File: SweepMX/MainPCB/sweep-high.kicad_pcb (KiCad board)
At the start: 2 copper layers, 229.5 x 95.2 mm, 61 parts, among them J1 AudioJack4dpb, J2 AudioJack4dpb, SW10 SW_Push, SW10_r1 SW_Push, SW11 SW_Push, SW11_r1 SW_Push, SW12 SW_Push, SW12_r1 SW_Push, SW13_r1 SW_Push, SW14 SW_Push, SW14_r1 SW_Push, SW15 SW_Push, SW15_r1 SW_Push, SW16 SW_Push, SW16_r1 SW_Push, SW17 SW_Push, SW17_r1 SW_Push, SW18 SW_Push, SW18_r1 SW_Push, SW2 SW_Push, SW20 SW_Push, SW21 SW_Push, SW2_r1 SW_Push, SW3 SW_Push, SW3_r1 SW_Push, SW4 SW_Push, SW4_r1 SW_Push, SW5 SW_Push, SW5_r1 SW_Push, SW6 SW_Push, SW6_r1 SW_Push, SW7_r1 SW_Push, SW8 SW_Push, SW8_r1 SW_Push, SW9 SW_Push, SW9_r1 SW_Push, U1 ProMicro-kbd, U2 ProMicro-kbd

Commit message: rename of some bits and a couple missed fixes
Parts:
- moved J1 0.12 mm to (149.6, 121.8)
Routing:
- net Switch15: track 48.6 -> 56.1 mm
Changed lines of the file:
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@@
   )
   (footprint "env_extra:PJ-320A" (layer "F.Cu")
-    (at 149.55 121.925 180)
+    (at 149.55 121.8 180)
     (property "Sheetfile" "sweep-high.kicad_sch")
     (property "Sheetname" "")
@@
   )
   (footprint "env_extra:PJ-320A" (layer "F.Cu")
-    (at 150.975 117.45)
+    (at 150.975 117.4)
     (property "Sheetfile" "sweep-high.kicad_sch")
     (property "Sheetname" "")
@@
   (segment (start 146.160165 83.45) (end 146.160165 89.302765) (width 0.15) (layer "B.Cu") (net 2))
   (segment (start 146.160165 89.302765) (end 147.7054 90.848) (width 0.15) (layer "B.Cu") (net 2))
-  (segment (start 143.08 94.488) (end 143.08 100.76) (width 0.25) (layer "F.Cu") (net 3))
   (segment (start 140.56 103.28) (end 140.56 114.964) (width 0.25) (layer "F.Cu") (net 3))
-  (segment (start 142.064 93.472) (end 143.08 94.488) (width 0.25) (layer "F.Cu") (net 3))
+  (segment (start 143.08 100.76) (end 140.56 103.28) (width 0.25) (layer "F.Cu") (net 3))
   (segment (start 138.938 93.472) (end 142.064 93.472) (width 0.25) (layer "F.Cu") (net 3))
-  (segment (start 152.90924 93.388) (end 159.275 99.75376) (width 0.25) (layer "F.Cu") (net 3))
-  (segment (start 159.275 117.3) (end 159.125 117.45) (width 0.25) (layer "F.Cu") (net 3))
-  (segment (start 159.275 99.75376) (end 159.275 117.3) (width 0.25) (layer "F.Cu") (net 3))
+  (segment (start 142.064 93.472) (end 143.08 94.488) (width 0.25) (layer "F.Cu") (net 3))
   (segment (start 140.56 114.964) (end 141.225 115.629) (width 0.25) (layer "F.Cu") (net 3))
-  (segment (start 141.225 115.629) (end 141.225 121.75) (width 0.25) (layer "F.Cu") (net 3))
-  (segment (start 141.225 121.75) (end 141.4 121.925) (width 0.25) (layer "F.Cu") (net 3))
-  (segment (start 143.08 100.76) (end 140.56 103.28) (width 0.25) (layer "F.Cu") (net 3))
+  (segment (start 152.90924 93.388) (end 159.275 99.75376) (width 0.25) (layer "F.Cu") (net 3))
+  (segment (start 141.225 115.629) (end 141.225 121.625) (width 0.25) (layer "F.Cu") (net 3))
+  (segment (start 159.275 99.75376) (end 159.275 117.25) (width 0.25) (layer "F.Cu") (net 3))
+  (segment (start 141.225 121.625) (end 141.4 121.8) (width 0.25) (layer "F.Cu") (net 3))
+  (segment (start 159.275 117.25) (end 159.125 117.4) (width 0.25) (layer "F.Cu") (net 3))
+  (segment (start 143.08 94.488) (end 143.08 100.76) (width 0.25) (layer "F.Cu") (net 3))
   (via (at 138.938 93.472) (size 0.6) (drill 0.35) (layers "F.Cu" "B.Cu") (net 3))
   (segment (start 138.938 93.472) (end 138.854 93.388) (width 0.25) (layer "B.Cu") (net 3))
   (segment (start 138.854 93.388) (end 132.4854 93.388) (width 0.25) (layer "B.Cu") (net 3))
   (segment (start 140.038 88.308) (end 147.7054 88.308) (width 0.25) (layer "F.Cu") (net 4))
-  (segment (start 136.4 117.525) (end 137.3 116.625) (width 0.25) (layer "F.Cu") (net 4))
+  (segment (start 136.4 117.4) (end 137.3 116.5) (width 0.25) (layer "F.Cu") (net 4))
   (segment (start 137.3 91.046) (end 140.038 88.308) (width 0.25) (layer "F.Cu") (net 4))
-  (segment (start 137.3 116.625) (end 137.3 91.046) (width 0.25) (layer "F.Cu") (net 4))
+  (segment (start 137.3 116.5) (end 137.3 91.046) (width 0.25) (layer "F.Cu") (net 4))
   (segment (start 127.45 116.5) (end 129.092 116.5) (width 0.25) (layer "F.Cu") (net 5))
   (segment (start 133.975 117.225) (end 129.575 117.225) (width 0.25) (layer "F.Cu") (net 5))
@@
   (segment (start 115.865685 115.94) (end 101.99 115.94) (width 0.25) (layer "B.Cu") (net 19))
   (segment (start 119.126 120.904) (end 119.126 114.696) (width 0.25) (layer "F.Cu") (net 20))
+  (segment (start 115.88 107.72) (end 117.8 105.8) (width 0.15) (layer "F.Cu") (net 20))
+  (segment (start 117.8 105.8) (end 117.8 102.098) (width 0.15) (layer "F.Cu") (net 20))
   (segment (start 115.88 111.45) (end 115.88 107.908) (width 0.25) (layer "F.Cu") (net 20))
+  (segment (start 117.8 102.098) (end 117.17 101.468) (width 0.15) (layer "F.Cu") (net 20))
   (segment (start 119.126 114.696) (end 115.88 111.45) (width 0.25) (layer "F.Cu") (net 20))
+  (segment (start 115.88 107.908) (end 115.88 107.72) (width 0.15) (layer "F.Cu") (net 20))
   (via (at 119.126 120.904) (size 0.6) (drill 0.35) (layers "F.Cu" "B.Cu") (net 20))
   (segment (start 129.825684 121.64) (end 142.837686 108.628) (width 0.25) (layer "B.Cu") (net 20))
@@
   (segment (start 160.53 87.53) (end 157.6 87.53) (width 0.25) (layer "B.Cu") (net 24))
   (segment (start 161.5 85.505) (end 161.5 86.56) (width 0.25) (layer "B.Cu") (net 24))
+  (segment (start 161.2 110.38) (end 161.2 117.075) (width 0.25) (layer "F.Cu") (net 25))
   (segment (start 164.9 91.53724) (end 168.12924 88.308) (width 0.25) (layer "F.Cu") (net 25))
+  (segment (start 163.575 119) (end 164.355 119.78) (width 0.25) (layer "F.Cu") (net 25))
   (segment (start 164.9 91.6) (end 164.9 91.53724) (width 0.25) (layer "F.Cu") (net 25))
-  (segment (start 161.2 110.38) (end 161.2 117.075) (width 0.25) (layer "F.Cu") (net 25))
-  (segment (start 163.125 119) (end 163.575 119) (width 0.25) (layer "F.Cu") (net 25))
+  (segment (start 164.355 121.57) (end 164.125 121.8) (width 0.25) (layer "F.Cu") (net 25))
   (segment (start 161.2 117.075) (end 163.125 119) (width 0.25) (layer "F.Cu") (net 25))
-  (segment (start 164.355 121.62) (end 164.125 121.85) (width 0.25) (layer "F.Cu") (net 25))
-  (segment (start 164.355 119.78) (end 164.355 121.62) (width 0.25) (layer "F.Cu") (net 25))
-  (segment (start 163.575 119) (end 164.355 119.78) (width 0.25) (layer "F.Cu") (net 25))
+  (segment (start 164.355 119.78) (end 164.355 121.57) (width 0.25) (layer "F.Cu") (net 25))
+  (segment (start 163.125 119) (end 163.575 119) (width 0.25) (layer "F.Cu") (net 25))
   (segment (start 161.225 110.355) (end 161.2 110.38) (width 0.25) (layer "F.Cu") (net 25))
   (via (at 164.9 91.6) (size 0.6) (drill 0.35) (layers "F.Cu" "B.Cu") (net 25))

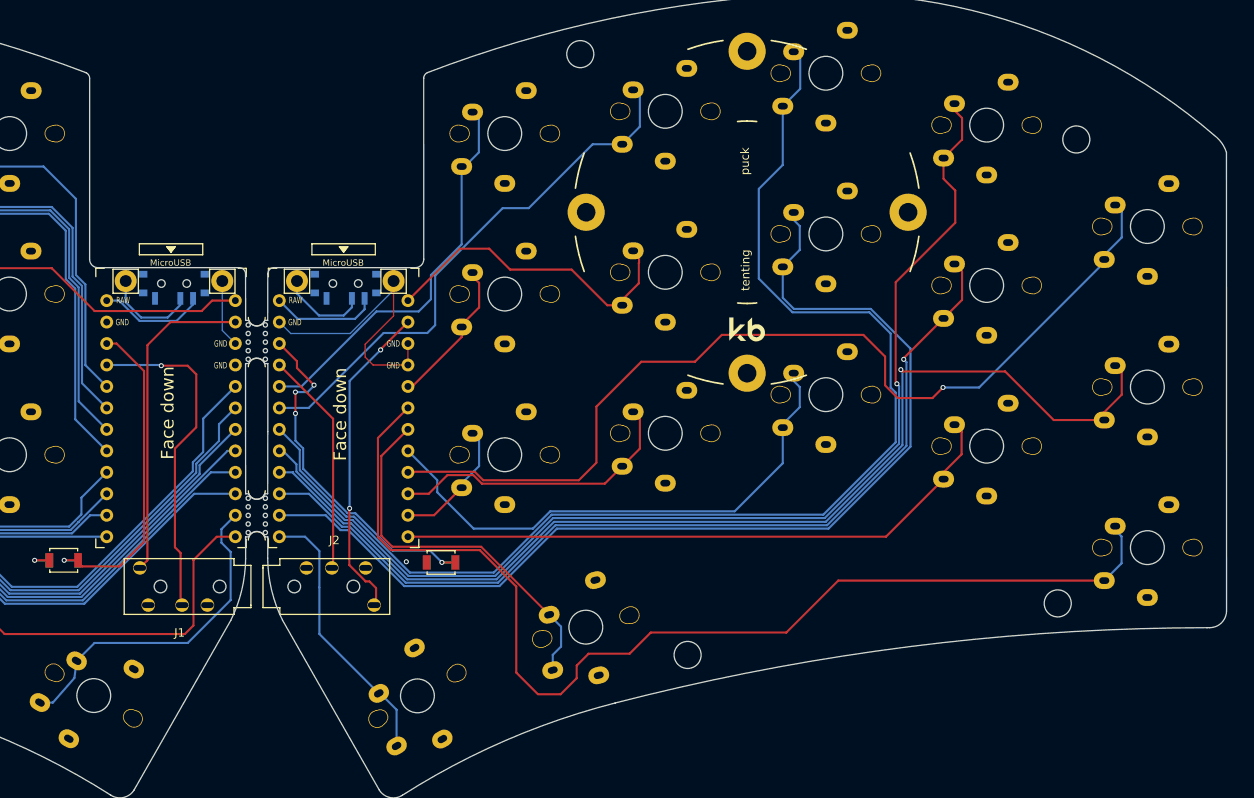
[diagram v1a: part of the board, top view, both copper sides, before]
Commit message: sorted schematic and PCB for MX ver
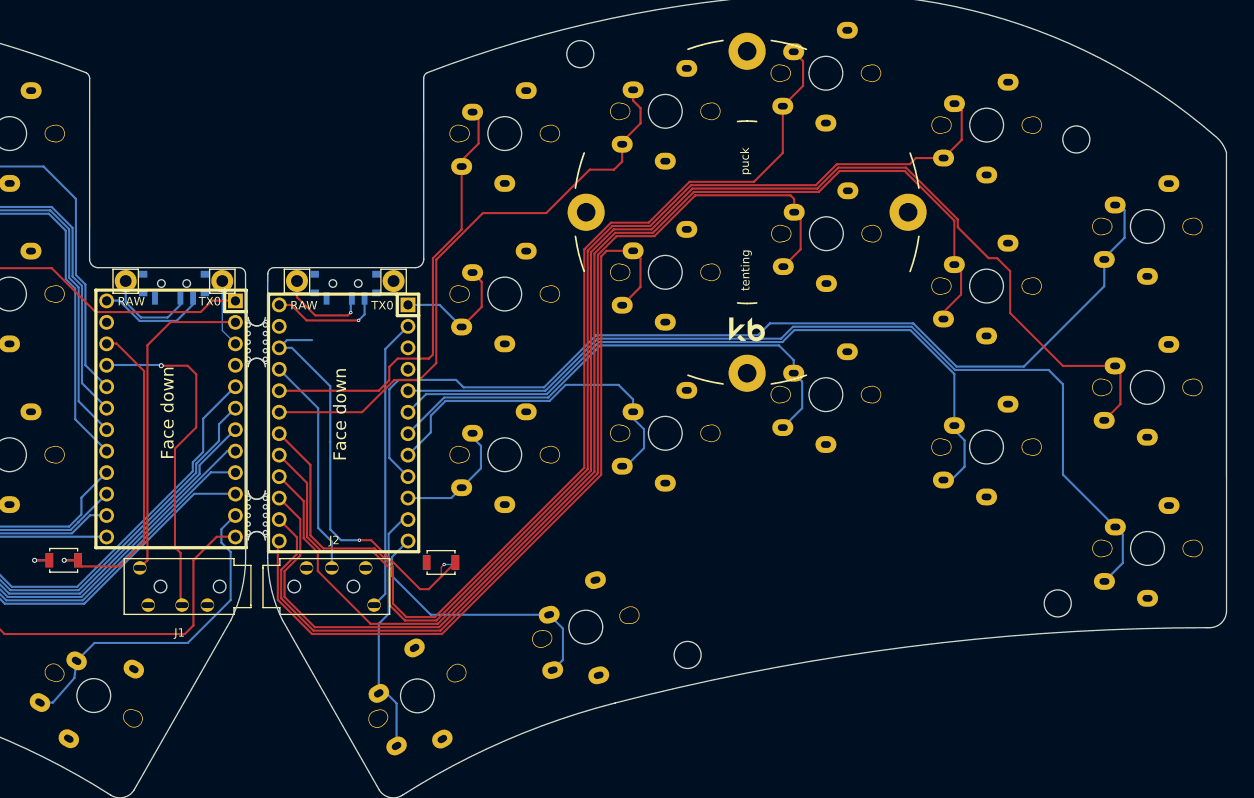
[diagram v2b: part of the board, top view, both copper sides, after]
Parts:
- removed SW13_r1, SW7_r1: SW_Push, kbd:CherryMX_Choc_1u
- added SW10_r1: SW_Push, kbd:CherryMX_Choc_1u, F.Cu at (217.7, 77.8)
- added SW14_r1: SW_Push, kbd:CherryMX_Choc_1u, F.Cu at (255.7, 115.1)
- U1, U2: footprint kbd:ProMicro_v3_min -> Keebio-Parts:ArduinoProMicro-BackSide; moved to B.Cu
- moved SW18_r1 57.0 mm to (179.6, 104.0)
- moved SW8_r1 22.5 mm to (255.6, 96.0)
- moved SW15_r1 20.0 mm to (236.6, 103.1)
- moved SW9_r1 20.0 mm to (236.6, 84.0)
- moved SW16_r1 19.5 mm to (217.6, 96.9)
- moved SW17_r1 19.2 mm to (198.6, 101.5)
- moved U1 0.47 mm to (140.1, 99.8), turned to -90 degrees
- turned U2 to -90 degrees
- renumbered SW10_r1 to SW20_r1, SW14_r1 to SW21_r1
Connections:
- SW11_r1 pad 1: Switch10_r -> Switch9_r
- SW12_r1 pad 1: Switch11_r -> Switch10_r
- SW15_r1 pad 1: Switch14_r -> Switch12_r
- SW16_r1 pad 1: Switch15_r -> Switch13_r
- SW17_r1 pad 1: Switch16_r -> Switch14_r
- SW18_r1 pad 1: Switch17_r -> Switch15_r
- SW20_r1 pad 1: Switch9_r -> Switch16_r
- SW21_r1 pad 1: Switch13_r -> Switch17_r
- SW8_r1 pad 1: Switch7_r -> Switch6_r
- SW9_r1 pad 1: Switch8_r -> Switch7_r
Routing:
- net Switch11_r: track 17.6 -> 110.6 mm
- net Switch9_r: track 32.4 -> 92.4 mm
- net Switch12_r: track 130.4 -> 85.5 mm
- net Switch17_r: track 73.9 -> 33.1 mm
- net Switch6_r: track 128.8 -> 168.2 mm, vias 1 -> 0
- net Switch7_r: track 110.2 -> 147.0 mm, vias 1 -> 0
- net gnd: track 47.2 -> 11.5 mm, vias 2 -> 1
- net Switch10_r: track 38.2 -> 15.3 mm
- net Switch14_r: track 64.0 -> 41.7 mm
- net Switch3_r: track 148.4 -> 127.4 mm
- net Switch15_r: track 35.2 -> 14.7 mm
- net Switch13_r: track 45.2 -> 60.0 mm
- net Switch16_r: track 15.3 -> 30.0 mm
- net reset_r: track 42.9 -> 51.2 mm, vias 4 -> 2
- net Switch2_r: track 131.6 -> 138.5 mm, vias 1 -> 0
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
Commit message: re-worked choc version
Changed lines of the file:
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@@
   (segment (start 214.6 79.7) (end 214.6 76.07) (width 0.25) (layer "F.Cu") (net 43))
   (segment (start 156.945686 124.82) (end 171.984314 124.82) (width 0.25) (layer "F.Cu") (net 43))
-  (zone (net 2) (net_name "gnd") (layer "F.Cu") (hatch edge 0.508)
+  (zone (net 2) (net_name "gnd") (layers F&B.Cu) (hatch edge 0.508)
     (connect_pads (clearance 0.508))
     (min_thickness 0.254) (filled_areas_thickness no)
@@
       (pts
         (xy 27.94 38.1)
-        (xy 271.78 38.1)
-        (xy 271.78 157.48)
+        (xy 275.7424 38.1)
+        (xy 275.7424 157.48)
         (xy 27.94 157.48)
       )
     )
-  )
-  (zone (net 2) (net_name "gnd") (layer "B.Cu") (hatch edge 0.508)
-    (connect_pads (clearance 0.508))
-    (min_thickness 0.254) (filled_areas_thickness no)
-    (fill yes (thermal_gap 0.508) (thermal_bridge_width 0.508))
-    (polygon
-      (pts
-        (xy 25.4 35.56)
-        (xy 274.32 35.56)
-        (xy 274.32 160.02)
-        (xy 25.4 160.02)
-      )
-    )
